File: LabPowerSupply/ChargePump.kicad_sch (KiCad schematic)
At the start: 6 parts

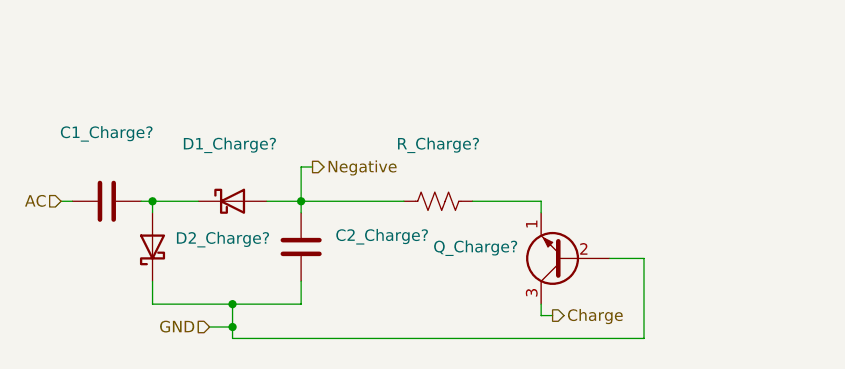
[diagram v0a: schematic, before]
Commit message: Finished first pass on the schematic
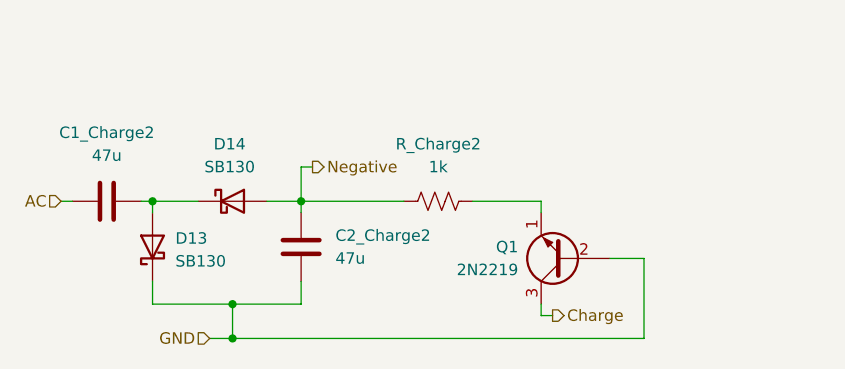
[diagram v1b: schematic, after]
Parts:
- removed D1_Charge?, D2_Charge?: ~, symbol Diode:SB130
- removed Q_Charge?: ~, symbol Transistor_BJT:2N2219
- added D13, D14: SB130, Diode_THT:D_DO-41_SOD81_P10.16mm_Horizontal, symbol Diode:SB130
- added Q1: 2N2219, Package_TO_SOT_THT:TO-39-3, symbol Transistor_BJT:2N2219
- C1_Charge2: renamed from C1_Charge?; value ~ -> 47u; footprint (none) -> Capacitor_SMD:C_1210_3225Metric
- C2_Charge2: renamed from C2_Charge?; value ~ -> 47u; footprint (none) -> Capacitor_SMD:C_1210_3225Metric
- R_Charge2: renamed from R_Charge?; value ~ -> 1k; footprint (none) -> Resistor_SMD:R_1210_3225Metric
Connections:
- net Charge: now also Q1.3 (C)
- net GND: now also D13.1 (K), Q1.2 (B)
- net Negative: now also D14.2 (A)
- net at C1_Charge2.2: now also D13.2 (A), D14.1 (K)
- net at R_Charge2.2: now also Q1.1 (E)
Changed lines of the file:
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@@
     (company "George Mason University")
   )
-  (junction (at 137.16 114.3) (diameter 0) (color 0 0 0 0)
+  (junction (at 137.16 115.57) (diameter 0) (color 0 0 0 0)
   )
   (junction (at 137.16 111.76) (diameter 0) (color 0 0 0 0)
@@
     (stroke (width 0) (type default) (color 0 0 0 0))
   )
-  (wire (pts (xy 137.16 114.3) (xy 137.16 111.76))
+  (wire (pts (xy 137.16 111.76) (xy 137.16 115.57))
     (stroke (width 0) (type default) (color 0 0 0 0))
   )
   (wire (pts (xy 144.78 100.33) (xy 156.21 100.33))
-    (stroke (width 0) (type default) (color 0 0 0 0))
-  )
-  (wire (pts (xy 137.16 115.57) (xy 137.16 114.3))
     (stroke (width 0) (type default) (color 0 0 0 0))
   )
@@
     (stroke (width 0) (type default) (color 0 0 0 0))
   )
-  (wire (pts (xy 134.62 114.3) (xy 137.16 114.3))
+  (wire (pts (xy 134.62 115.57) (xy 137.16 115.57))
     (stroke (width 0) (type default) (color 0 0 0 0))
   )
@@
     (stroke (width 0) (type default) (color 0 0 0 0))
   )
-  (hierarchical_label "GND" (shape input) (at 134.62 114.3 180)
+  (hierarchical_label "GND" (shape input) (at 134.62 115.57 180)
     (effects (font (size 1.27 1.27)) (justify right))
   )
@@
   (symbol (lib_id "Device:C") (at 144.78 105.41 0) (unit 1)
     (in_bom yes) (on_board yes) (fields_autoplaced)
-    (property "Reference" "C2_Charge?" (id 0) (at 148.59 104.1399 0)
+    (property "Reference" "C2_Charge2" (id 0) (at 148.59 104.1399 0)
       (effects (font (size 1.27 1.27)) (justify left))
     )
-    (property "Value" "~" (id 1) (at 148.59 106.6799 0)
+    (property "Value" "47u" (id 1) (at 148.59 106.6799 0)
       (effects (font (size 1.27 1.27)) (justify left))
     )
-    (property "Footprint" "" (id 2) (at 145.7452 109.22 0)
+    (property "Footprint" "Capacitor_SMD:C_1210_3225Metric" (id 2) (at 145.7452 109.22 0)
       (effects (font (size 1.27 1.27)) hide)
     )
@@
   (symbol (lib_id "Device:C") (at 123.19 100.33 90) (unit 1)
     (in_bom yes) (on_board yes) (fields_autoplaced)
-    (property "Reference" "C1_Charge?" (id 0) (at 123.19 92.71 90))
-    (property "Value" "~" (id 1) (at 123.19 95.25 90))
-    (property "Footprint" "" (id 2) (at 127 99.3648 0)
+    (property "Reference" "C1_Charge2" (id 0) (at 123.19 92.71 90))
+    (property "Value" "47u" (id 1) (at 123.19 95.25 90))
+    (property "Footprint" "Capacitor_SMD:C_1210_3225Metric" (id 2) (at 127 99.3648 0)
       (effects (font (size 1.27 1.27)) hide)
     )
@@
   (symbol (lib_id "Diode:SB130") (at 128.27 105.41 90) (unit 1)
     (in_bom yes) (on_board yes) (fields_autoplaced)
-    (property "Reference" "D2_Charge?" (id 0) (at 130.81 104.4574 90)
+    (property "Reference" "D13" (id 0) (at 130.81 104.4574 90)
       (effects (font (size 1.27 1.27)) (justify right))
     )
-    (property "Value" "~" (id 1) (at 130.81 106.9974 90)
+    (property "Value" "SB130" (id 1) (at 130.81 106.9974 90)
       (effects (font (size 1.27 1.27)) (justify right))
     )
-    (property "Footprint" "" (id 2) (at 132.715 105.41 0)
+    (property "Footprint" "Diode_THT:D_DO-41_SOD81_P10.16mm_Horizontal" (id 2) (at 132.715 105.41 0)
       (effects (font (size 1.27 1.27)) hide)
     )
@@
   (symbol (lib_id "Transistor_BJT:2N2219") (at 173.99 106.68 180) (unit 1)
     (in_bom yes) (on_board yes) (fields_autoplaced)
-    (property "Reference" "Q_Charge?" (id 0) (at 168.91 105.4099 0)
+    (property "Reference" "Q1" (id 0) (at 168.91 105.4099 0)
       (effects (font (size 1.27 1.27)) (justify left))
     )
-    (property "Value" "~" (id 1) (at 168.91 107.9499 0)
+    (property "Value" "2N2219" (id 1) (at 168.91 107.9499 0)
       (effects (font (size 1.27 1.27)) (justify left))
     )
-    (property "Footprint" "" (id 2) (at 168.91 104.775 0)
+    (property "Footprint" "Package_TO_SOT_THT:TO-39-3" (id 2) (at 168.91 104.775 0)
       (effects (font (size 1.27 1.27) italic) (justify left) hide)
     )
@@
     (pin "3")
   )
+  (symbol (lib_id "Diode:SB130") (at 137.16 100.33 0) (unit 1)
+    (in_bom yes) (on_board yes) (fields_autoplaced)
+    (property "Reference" "D14" (id 0) (at 136.8425 93.98 0))
+    (property "Value" "SB130" (id 1) (at 136.8425 96.52 0))
+    (property "Footprint" "Diode_THT:D_DO-41_SOD81_P10.16mm_Horizontal" (id 2) (at 137.16 104.775 0)
+      (effects (font (size 1.27 1.27)) hide)
+    )
+    (property "Datasheet" "http://www.diodes.com/_files/datasheets/ds23022.pdf" (id 3) (at 137.16 100.33 0)
+      (effects (font (size 1.27 1.27)) hide)
+    )
+    (pin "1")
+    (pin "2")
+  )
   (symbol (lib_id "Device:R_US") (at 160.02 100.33 90) (unit 1)
     (in_bom yes) (on_board yes) (fields_autoplaced)
-    (property "Reference" "R_Charge?" (id 0) (at 160.02 93.98 90))
-    (property "Value" "~" (id 1) (at 160.02 96.52 90))
-    (property "Footprint" "" (id 2) (at 160.274 99.314 90)
+    (property "Reference" "R_Charge2" (id 0) (at 160.02 93.98 90))
+    (property "Value" "1k" (id 1) (at 160.02 96.52 90))
+    (property "Footprint" "Resistor_SMD:R_1210_3225Metric" (id 2) (at 160.274 99.314 90)
       (effects (font (size 1.27 1.27)) hide)
     )
@@
       (effects (font (size 1.27 1.27)) hide)
     )
-    (pin "1")
-    (pin "2")
-  )
-  (symbol (lib_id "Diode:SB130") (at 137.16 100.33 0) (unit 1)
-    (in_bom yes) (on_board yes) (fields_autoplaced)
-    (property "Reference" "D1_Charge?" (id 0) (at 136.8425 93.98 0))
-    (property "Value" "~" (id 1) (at 136.8425 96.52 0))
-    (property "Footprint" "" (id 2) (at 137.16 104.775 0)
-      (effects (font (size 1.27 1.27)) hide)
-    )
-    (property "Datasheet" "http://www.diodes.com/_files/datasheets/ds23022.pdf" (id 3) (at 137.16 100.33 0)
-      (effects (font (size 1.27 1.27)) hide)
-    )

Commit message: started PCB
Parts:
- Q2: renamed from Q1; footprint Package_TO_SOT_THT:TO-39-3 -> Package_TO_SOT_THT:TO-92_Inline
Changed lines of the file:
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@@
   (symbol (lib_id "Transistor_BJT:2N2219") (at 173.99 106.68 180) (unit 1)
     (in_bom yes) (on_board yes) (fields_autoplaced)
-    (property "Reference" "Q1" (id 0) (at 168.91 105.4099 0)
+    (property "Reference" "Q2" (id 0) (at 168.91 105.4099 0)
       (effects (font (size 1.27 1.27)) (justify left))
     )
@@
       (effects (font (size 1.27 1.27)) (justify left))
     )
-    (property "Footprint" "Package_TO_SOT_THT:TO-39-3" (id 2) (at 168.91 104.775 0)
+    (property "Footprint" "Package_TO_SOT_THT:TO-92_Inline" (id 2) (at 168.91 104.775 0)
       (effects (font (size 1.27 1.27) italic) (justify left) hide)
     )

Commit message: more work
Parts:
- added C3_CP1: 1m, Capacitor_THT:CP_Radial_D10.0mm_P5.00mm, symbol Device:C_Polarized_US
- renumbered C1_Charge2 to C1_CP1, C2_Charge2 to C2_CP1, D14 to D1_CP1, D13 to D2_CP1, Q2 to Q_CP1, R_Charge2 to R_CP1
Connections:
- net GND: now also C3_CP1.1
- net Negative: now also C3_CP1.2
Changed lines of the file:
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@@
     (rev "1")
     (company "George Mason University")
+    (comment 1 "regulators so that they can stay in regulation.")
+    (comment 2 "reliably output 0V and to create a 1mA load for the linear")
+    (comment 3 "that can be tied to the op-amps' negative rail so that they can")
+    (comment 4 "The charge pump is used to generate a small negative voltage")
   )
   (junction (at 137.16 115.57) (diameter 0) (color 0 0 0 0)
   )
+  (junction (at 156.21 115.57) (diameter 0) (color 0 0 0 0)
+  )
+  (junction (at 156.21 100.33) (diameter 0) (color 0 0 0 0)
+  )
   (junction (at 137.16 111.76) (diameter 0) (color 0 0 0 0)
   )
@@
   (junction (at 128.27 100.33) (diameter 0) (color 0 0 0 0)
   )
-  (wire (pts (xy 137.16 115.57) (xy 182.88 115.57))
-    (stroke (width 0) (type default) (color 0 0 0 0))
-  )
   (wire (pts (xy 118.11 100.33) (xy 119.38 100.33))
     (stroke (width 0) (type default) (color 0 0 0 0))
@@
     (stroke (width 0) (type default) (color 0 0 0 0))
   )
+  (wire (pts (xy 137.16 115.57) (xy 156.21 115.57))
+    (stroke (width 0) (type default) (color 0 0 0 0))
+  )
+  (wire (pts (xy 137.16 111.76) (xy 144.78 111.76))
+    (stroke (width 0) (type default) (color 0 0 0 0))
+  )
+  (wire (pts (xy 182.88 106.68) (xy 182.88 115.57))
+    (stroke (width 0) (type default) (color 0 0 0 0))
+  )
   (wire (pts (xy 144.78 100.33) (xy 156.21 100.33))
     (stroke (width 0) (type default) (color 0 0 0 0))
   )
-  (wire (pts (xy 137.16 111.76) (xy 144.78 111.76))
-    (stroke (width 0) (type default) (color 0 0 0 0))
-  )
-  (wire (pts (xy 182.88 106.68) (xy 182.88 115.57))
-    (stroke (width 0) (type default) (color 0 0 0 0))
-  )
   (wire (pts (xy 128.27 111.76) (xy 137.16 111.76))
     (stroke (width 0) (type default) (color 0 0 0 0))
   )
+  (wire (pts (xy 156.21 115.57) (xy 182.88 115.57))
+    (stroke (width 0) (type default) (color 0 0 0 0))
+  )
   (wire (pts (xy 133.35 100.33) (xy 128.27 100.33))
     (stroke (width 0) (type default) (color 0 0 0 0))
@@
   )
   (wire (pts (xy 128.27 101.6) (xy 128.27 100.33))
+    (stroke (width 0) (type default) (color 0 0 0 0))
+  )
+  (wire (pts (xy 156.21 107.95) (xy 156.21 100.33))
     (stroke (width 0) (type default) (color 0 0 0 0))
   )
@@
   (symbol (lib_id "Device:C") (at 144.78 105.41 0) (unit 1)
     (in_bom yes) (on_board yes) (fields_autoplaced)
-    (property "Reference" "C2_Charge2" (id 0) (at 148.59 104.1399 0)
+    (property "Reference" "C2_CP1" (id 0) (at 148.59 104.1399 0)
       (effects (font (size 1.27 1.27)) (justify left))
     )
@@
   (symbol (lib_id "Device:C") (at 123.19 100.33 90) (unit 1)
     (in_bom yes) (on_board yes) (fields_autoplaced)
-    (property "Reference" "C1_Charge2" (id 0) (at 123.19 92.71 90))
+    (property "Reference" "C1_CP1" (id 0) (at 123.19 92.71 90))
     (property "Value" "47u" (id 1) (at 123.19 95.25 90))
     (property "Footprint" "Capacitor_SMD:C_1210_3225Metric" (id 2) (at 127 99.3648 0)
@@
   (symbol (lib_id "Diode:SB130") (at 128.27 105.41 90) (unit 1)
     (in_bom yes) (on_board yes) (fields_autoplaced)
-    (property "Reference" "D13" (id 0) (at 130.81 104.4574 90)
+    (property "Reference" "D2_CP1" (id 0) (at 130.81 104.4574 90)
       (effects (font (size 1.27 1.27)) (justify right))
     )
@@
   (symbol (lib_id "Transistor_BJT:2N2219") (at 173.99 106.68 180) (unit 1)
     (in_bom yes) (on_board yes) (fields_autoplaced)
-    (property "Reference" "Q2" (id 0) (at 168.91 105.4099 0)
+    (property "Reference" "Q_CP1" (id 0) (at 168.91 105.4099 0)
       (effects (font (size 1.27 1.27)) (justify left))
     )
@@
   (symbol (lib_id "Diode:SB130") (at 137.16 100.33 0) (unit 1)
     (in_bom yes) (on_board yes) (fields_autoplaced)
-    (property "Reference" "D14" (id 0) (at 136.8425 93.98 0))
+    (property "Reference" "D1_CP1" (id 0) (at 136.8425 93.98 0))
     (property "Value" "SB130" (id 1) (at 136.8425 96.52 0))
     (property "Footprint" "Diode_THT:D_DO-41_SOD81_P10.16mm_Horizontal" (id 2) (at 137.16 104.775 0)
@@
     (pin "2")
   )
+  (symbol (lib_id "Device:C_Polarized_US") (at 156.21 111.76 180) (unit 1)
+    (in_bom yes) (on_board yes) (fields_autoplaced)
+    (property "Reference" "C3_CP1" (id 0) (at 160.02 111.1249 0)
+      (effects (font (size 1.27 1.27)) (justify right))
+    )
+    (property "Value" "1m" (id 1) (at 160.02 113.6649 0)
+      (effects (font (size 1.27 1.27)) (justify right))
+    )
+    (property "Footprint" "Capacitor_THT:CP_Radial_D10.0mm_P5.00mm" (id 2) (at 156.21 111.76 0)
+      (effects (font (size 1.27 1.27)) hide)
+    )
+    (property "Datasheet" "~" (id 3) (at 156.21 111.76 0)
+      (effects (font (size 1.27 1.27)) hide)
+    )
+    (pin "1")
+    (pin "2")
+  )
   (symbol (lib_id "Device:R_US") (at 160.02 100.33 90) (unit 1)
     (in_bom yes) (on_board yes) (fields_autoplaced)
-    (property "Reference" "R_Charge2" (id 0) (at 160.02 93.98 90))
+    (property "Reference" "R_CP1" (id 0) (at 160.02 93.98 90))
     (property "Value" "1k" (id 1) (at 160.02 96.52 90))
     (property "Footprint" "Resistor_SMD:R_1210_3225Metric" (id 2) (at 160.274 99.314 90)

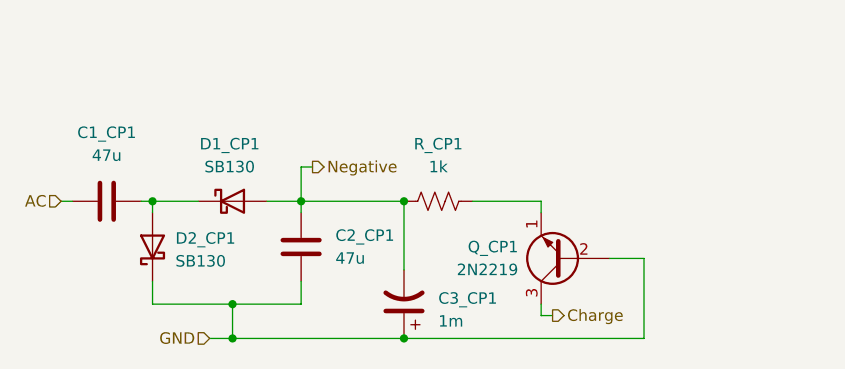
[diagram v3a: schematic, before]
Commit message: Resistor footprints changed to 0603
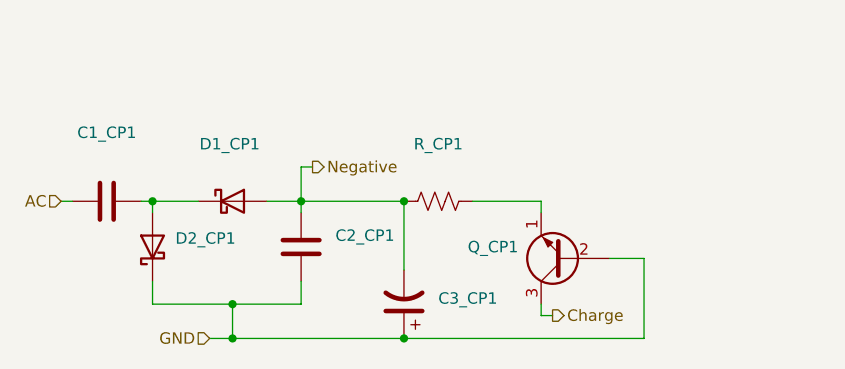
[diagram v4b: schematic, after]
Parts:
- C1_CP1, C2_CP1: value 47u -> (none); footprint Capacitor_SMD:C_1210_3225Metric -> (none)
- C3_CP1: value 1m -> (none); footprint Capacitor_THT:CP_Radial_D10.0mm_P5.00mm -> (none)
- D1_CP1, D2_CP1: value SB130 -> (none); footprint Diode_THT:D_DO-41_SOD81_P10.16mm_Horizontal -> (none)
- Q_CP1: value 2N2219 -> (none); footprint Package_TO_SOT_THT:TO-92_Inline -> (none)
- R_CP1: value 1k -> (none); footprint Resistor_SMD:R_1210_3225Metric -> (none)
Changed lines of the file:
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@@
       (effects (font (size 1.27 1.27)) (justify left))
     )
-    (property "Value" "47u" (id 1) (at 148.59 106.6799 0)
+    (property "Value" "" (id 1) (at 148.59 106.6799 0)
       (effects (font (size 1.27 1.27)) (justify left))
     )
-    (property "Footprint" "Capacitor_SMD:C_1210_3225Metric" (id 2) (at 145.7452 109.22 0)
+    (property "Footprint" "" (id 2) (at 145.7452 109.22 0)
       (effects (font (size 1.27 1.27)) hide)
     )
@@
     (in_bom yes) (on_board yes) (fields_autoplaced)
     (property "Reference" "C1_CP1" (id 0) (at 123.19 92.71 90))
-    (property "Value" "47u" (id 1) (at 123.19 95.25 90))
-    (property "Footprint" "Capacitor_SMD:C_1210_3225Metric" (id 2) (at 127 99.3648 0)
+    (property "Value" "" (id 1) (at 123.19 95.25 90))
+    (property "Footprint" "" (id 2) (at 127 99.3648 0)
       (effects (font (size 1.27 1.27)) hide)
     )
@@
       (effects (font (size 1.27 1.27)) (justify right))
     )
-    (property "Value" "SB130" (id 1) (at 130.81 106.9974 90)
+    (property "Value" "" (id 1) (at 130.81 106.9974 90)
       (effects (font (size 1.27 1.27)) (justify right))
     )
-    (property "Footprint" "Diode_THT:D_DO-41_SOD81_P10.16mm_Horizontal" (id 2) (at 132.715 105.41 0)
+    (property "Footprint" "" (id 2) (at 132.715 105.41 0)
       (effects (font (size 1.27 1.27)) hide)
     )
@@
       (effects (font (size 1.27 1.27)) (justify left))
     )
-    (property "Value" "2N2219" (id 1) (at 168.91 107.9499 0)
+    (property "Value" "" (id 1) (at 168.91 107.9499 0)
       (effects (font (size 1.27 1.27)) (justify left))
     )
-    (property "Footprint" "Package_TO_SOT_THT:TO-92_Inline" (id 2) (at 168.91 104.775 0)
+    (property "Footprint" "" (id 2) (at 168.91 104.775 0)
       (effects (font (size 1.27 1.27) italic) (justify left) hide)
     )
@@
     (in_bom yes) (on_board yes) (fields_autoplaced)
     (property "Reference" "D1_CP1" (id 0) (at 136.8425 93.98 0))
-    (property "Value" "SB130" (id 1) (at 136.8425 96.52 0))
-    (property "Footprint" "Diode_THT:D_DO-41_SOD81_P10.16mm_Horizontal" (id 2) (at 137.16 104.775 0)
+    (property "Value" "" (id 1) (at 136.8425 96.52 0))
+    (property "Footprint" "" (id 2) (at 137.16 104.775 0)
       (effects (font (size 1.27 1.27)) hide)
     )
@@
       (effects (font (size 1.27 1.27)) (justify right))
     )
-    (property "Value" "1m" (id 1) (at 160.02 113.6649 0)
+    (property "Value" "" (id 1) (at 160.02 113.6649 0)
       (effects (font (size 1.27 1.27)) (justify right))
     )
-    (property "Footprint" "Capacitor_THT:CP_Radial_D10.0mm_P5.00mm" (id 2) (at 156.21 111.76 0)
+    (property "Footprint" "" (id 2) (at 156.21 111.76 0)
       (effects (font (size 1.27 1.27)) hide)
     )
@@
     (in_bom yes) (on_board yes) (fields_autoplaced)
     (property "Reference" "R_CP1" (id 0) (at 160.02 93.98 90))
-    (property "Value" "1k" (id 1) (at 160.02 96.52 90))
-    (property "Footprint" "Resistor_SMD:R_1210_3225Metric" (id 2) (at 160.274 99.314 90)
+    (property "Value" "" (id 1) (at 160.02 96.52 90))
+    (property "Footprint" "" (id 2) (at 160.274 99.314 90)
       (effects (font (size 1.27 1.27)) hide)
     )
